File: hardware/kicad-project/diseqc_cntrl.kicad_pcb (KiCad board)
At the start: 4 copper layers, 90 x 100 mm, 124 parts, among them IC1 TPS560200DBVR, IC2 STM32F407VGT6, IC3 USBLC6-2P6, IC4 FM24CL16B-GTR, IC5 LNBH26PQR, IC6 W5500, J1 Barrel Jack, J2 Conn_01x04_Pin, J3 Conn_01x04_Pin, J4 USB4110-GF-A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

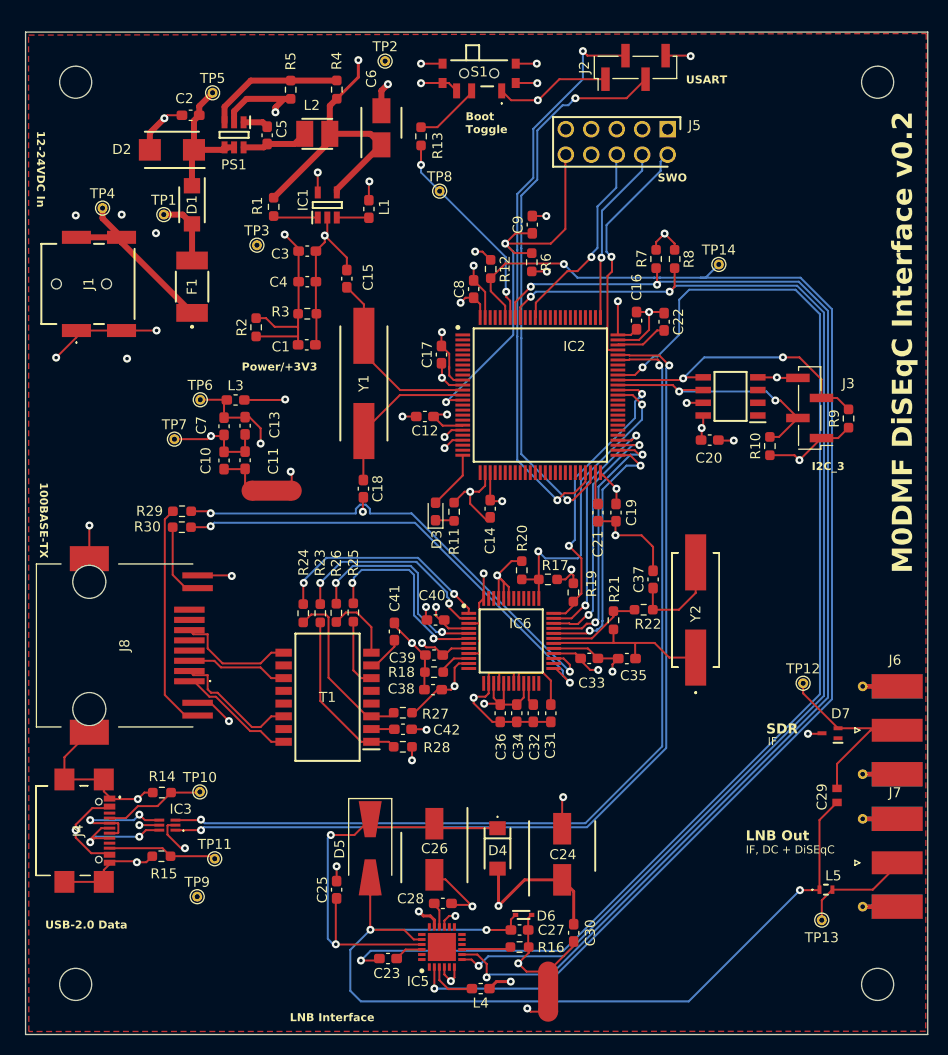
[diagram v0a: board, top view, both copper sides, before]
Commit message: Fixed pin conflict: TIM1_CH1/I2C3_SCL
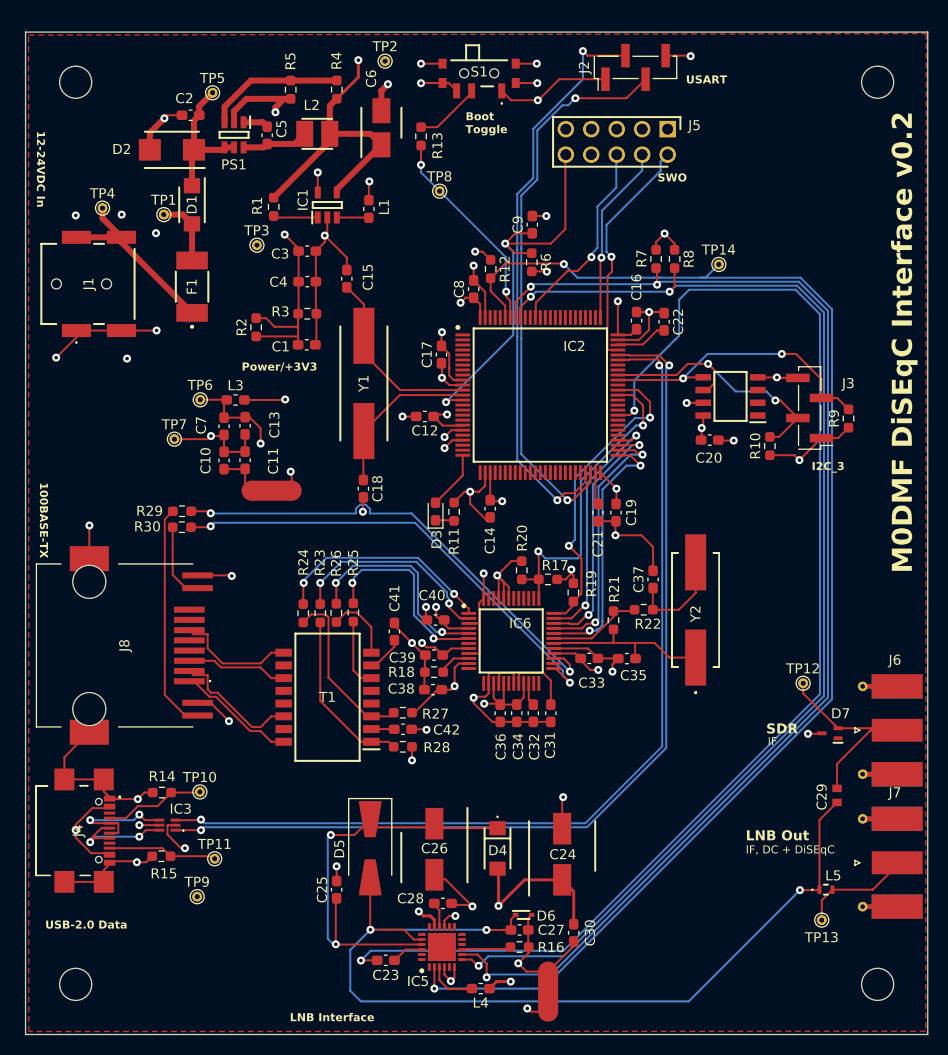
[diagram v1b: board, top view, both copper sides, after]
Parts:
- moved C23 0.28 mm to (85.9, 142.6), turned to 180 degrees
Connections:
- C23 pad 1: Net-(IC2-PA8) -> /MCU/LNBH26PQR/DISEQC
- C23 pad 2: /MCU/TIM1_CH1_DSQ -> /MCU/TIM4_CH1
- IC2 pad 59: unconnected-(IC2-PD12-Pad59) -> /MCU/TIM4_CH1
- IC2 pad 65: /MCU/I2C3_SCL -> unconnected-(IC2-PC8-Pad65)
- IC2 pad 67: Net-(IC2-PA8) -> /MCU/I2C3_SCL
- IC5 pad 22: /MCU/TIM1_CH1_DSQ -> /MCU/LNBH26PQR/DISEQC
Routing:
- net /MCU/TIM4_CH1: track 0.00 -> 127.0 mm, vias 0 -> 2
- net Net-(IC2-PA8): track 123.4 -> 0.00 mm, vias 2 -> 0
- net /MCU/TIM1_CH1_DSQ: track 2.89 -> 0.00 mm
- net /MCU/LNBH26PQR/DISEQC: track 0.00 -> 2.89 mm
- net /MCU/I2C3_SCL: track 25.4 -> 27.8 mm
- net /MCU/W5500 Ethernet/W5500_INT: track 29.6 -> 31.0 mm

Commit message: Grounded additional pins on IC5 & cleaned up track routing
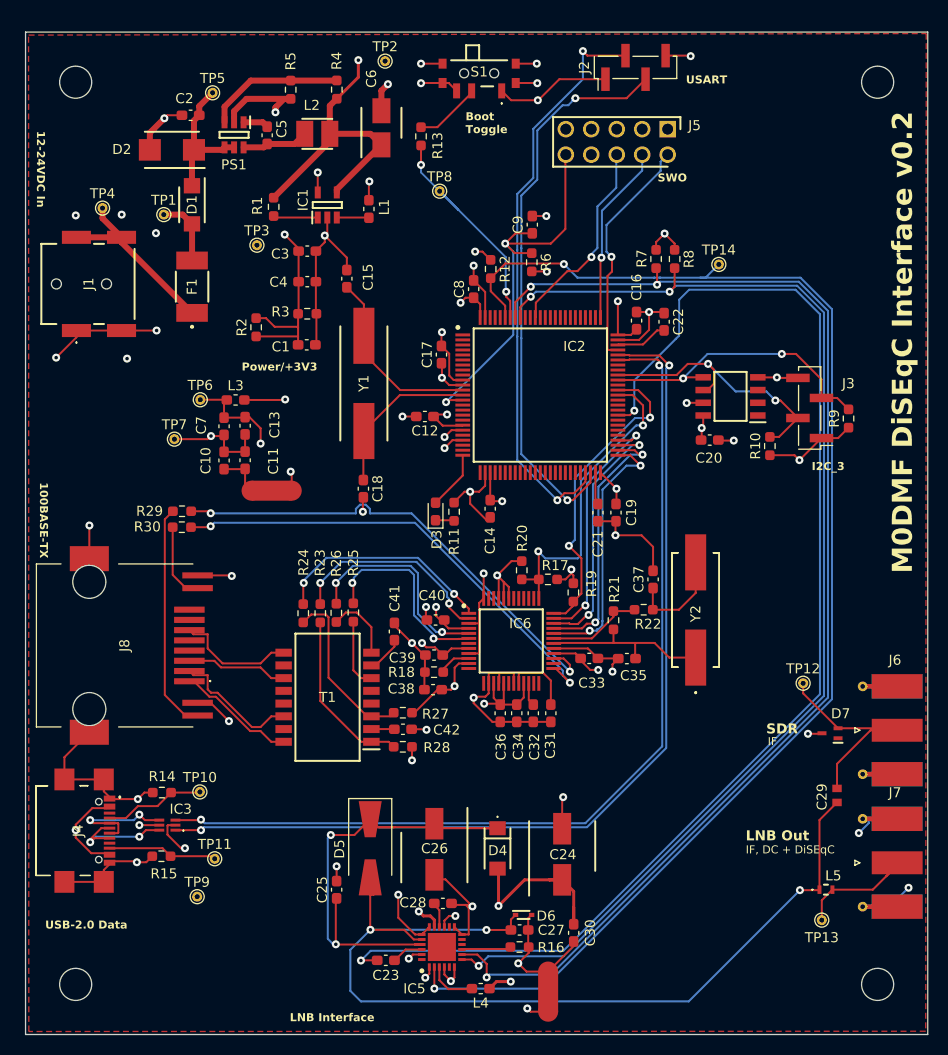
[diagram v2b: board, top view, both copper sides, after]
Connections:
- IC5 pad 1: unconnected-(IC5-DSQOUT_-B-Pad1) -> PGND
- IC5 pad 12: unconnected-(IC5-DETIN-B-Pad12) -> PGND
- IC5 pad 13: unconnected-(IC5-BPSW-B-Pad13) -> PGND
- IC5 pad 18: unconnected-(IC5-BPSW-A-Pad18) -> PGND
- IC5 pad 19: unconnected-(IC5-DETIN-A-Pad19) -> PGND
- IC5 pad 23: unconnected-(IC5-DSQOUT-A-Pad23) -> PGND
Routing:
- net PGND: track 24.7 -> 40.3 mm, vias 4 -> 7
- net GND: track 216.0 -> 230.3 mm, vias 41 -> 43
- net Net-(D4-K): track 42.1 -> 47.1 mm
- net +12V: track 201.2 -> 204.2 mm
- net /MCU/BOOT0: track 20.8 -> 23.4 mm
- net LNB_OUT: track 11.3 -> 13.1 mm
- net IF_OUT: track 23.3 -> 22.2 mm
- net VBUS: track 33.6 -> 34.3 mm
- net TX+: track 12.6 -> 11.9 mm
- net USB_D-: track 95.3 -> 94.7 mm
- net /MCU/W5500 Ethernet/W5500_INT: track 31.0 -> 31.5 mm
- net /MCU/LNBH26PQR/DISEQC: track 2.89 -> 3.41 mm

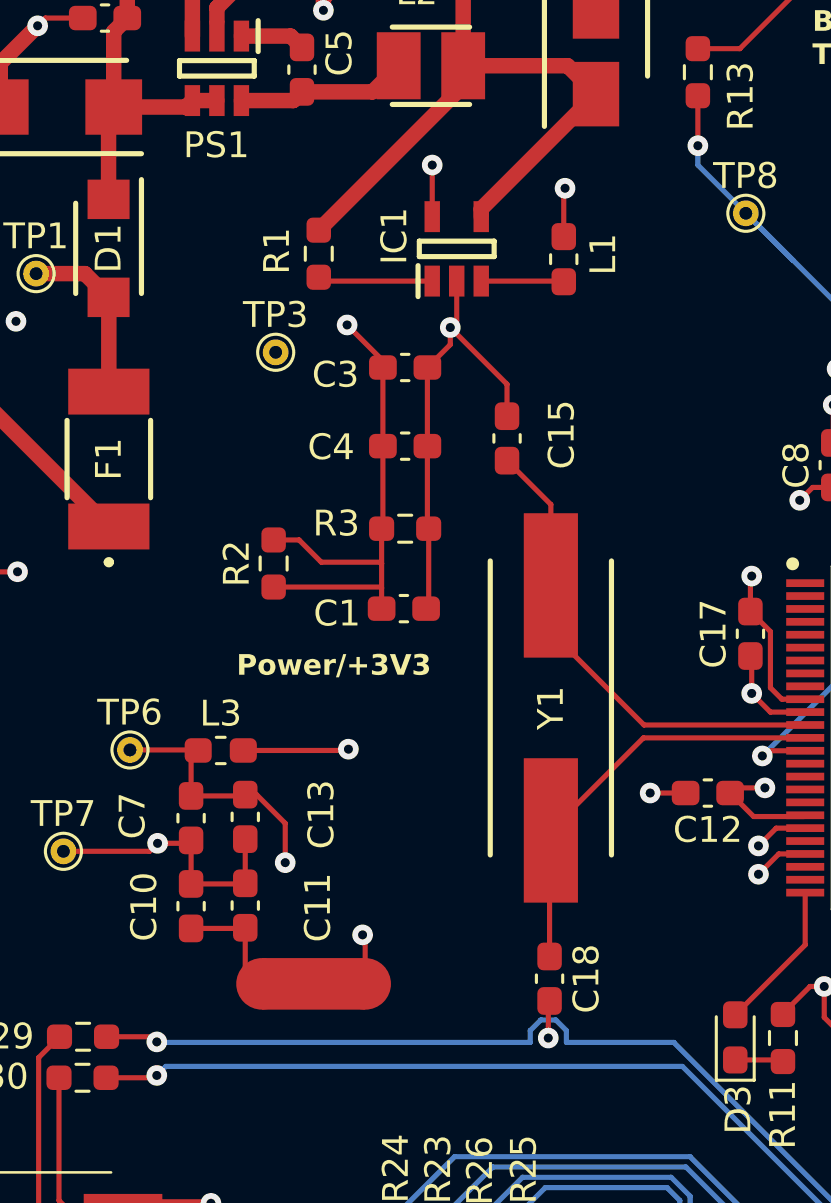
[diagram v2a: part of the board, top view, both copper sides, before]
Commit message: Corrected 3v3 reg component layout
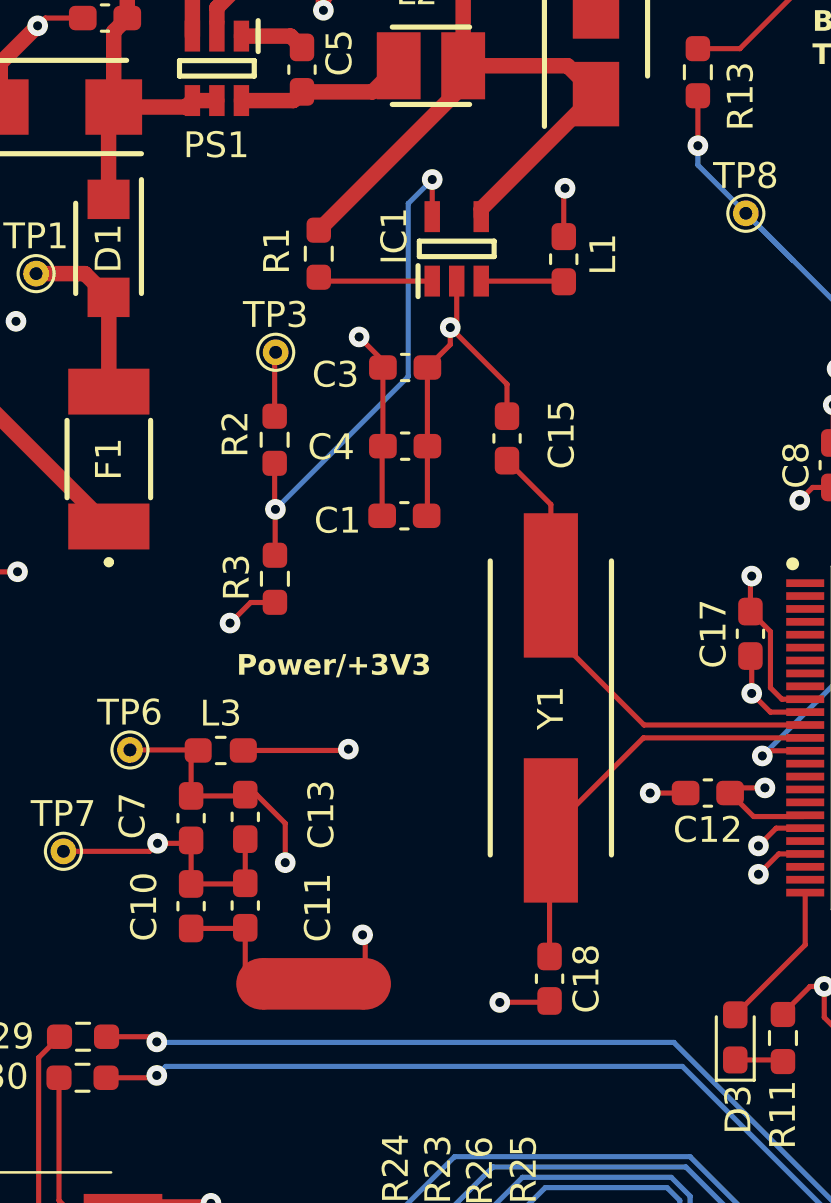
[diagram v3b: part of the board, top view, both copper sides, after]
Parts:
- moved R3 5.41 mm to (73.0, 80.0), turned to -90 degrees
- moved R2 4.80 mm to (73.0, 74.7), turned to -90 degrees
- moved C1 3.60 mm to (78.1, 77.6)
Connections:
- IC1 pad 5: +3V3 -> Net-(IC1-VSENSE)
- R2 pad 2: +3V3 -> Net-(IC1-VSENSE)
- R3 pad 1: +3V3 -> Net-(IC1-VSENSE)
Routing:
- net Net-(IC1-VSENSE): track 0.00 -> 20.4 mm, vias 0 -> 2
- net +3V3: track 145.1 -> 132.8 mm, vias 26 -> 25
- net /MCU/W5500 Ethernet/ACTLED: track 48.3 -> 47.0 mm
- net GND: track 230.3 -> 229.2 mm, vias 43 -> 44

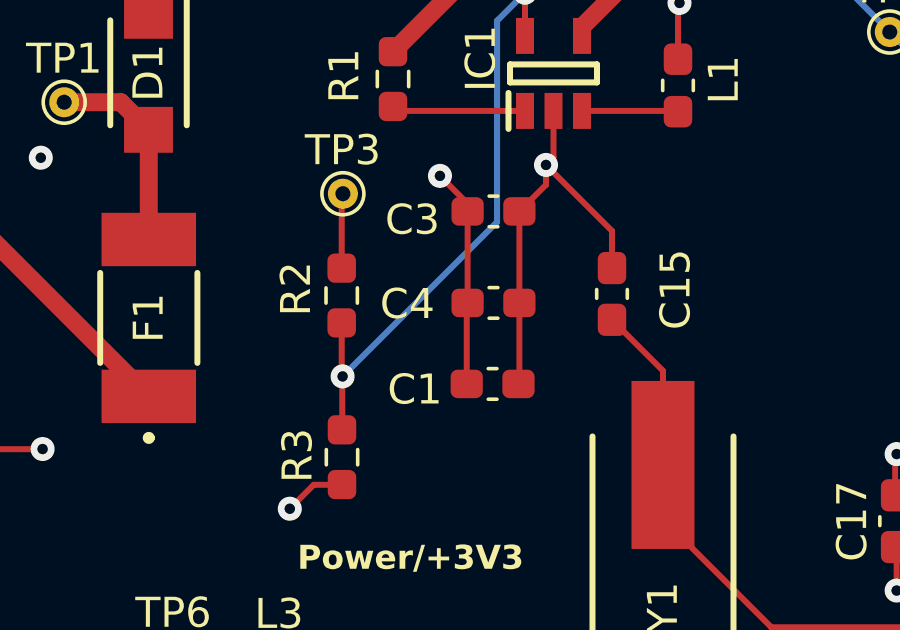
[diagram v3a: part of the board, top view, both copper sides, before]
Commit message: Removed/rerouted optional component C4
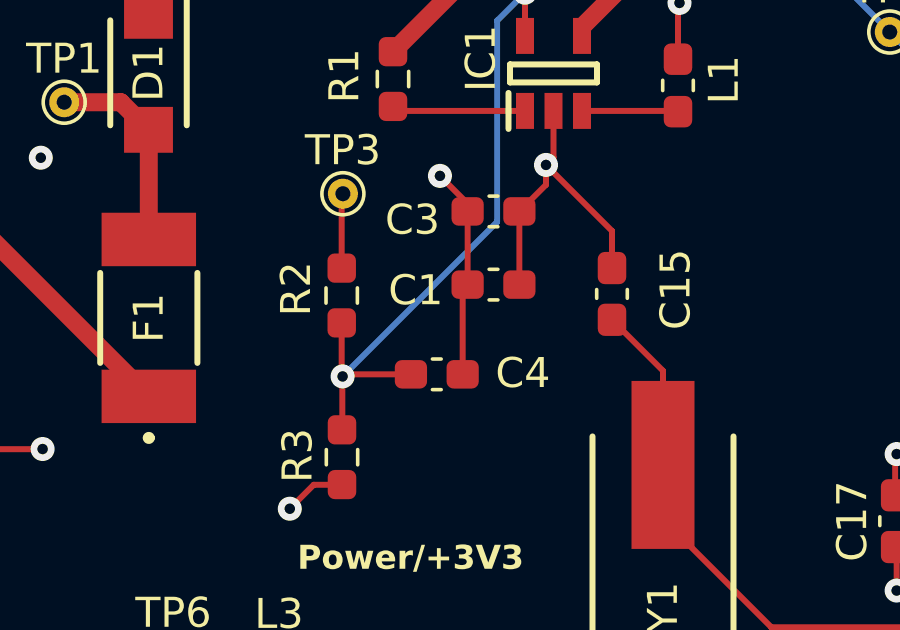
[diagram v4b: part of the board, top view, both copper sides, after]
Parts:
- C4: value 1u -> 22pF DNP
- moved C1 3.31 mm to (78.1, 74.3)
- moved C4 3.04 mm to (76.2, 77.3), turned to 180 degrees
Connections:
- C4 pad 2: GND -> Net-(IC1-VSENSE)
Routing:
- net GND: track 229.2 -> 225.9 mm
- net Net-(IC1-VSENSE): track 20.4 -> 22.7 mm
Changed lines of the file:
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@@
 	(footprint "Capacitor_SMD:C_0603_1608Metric_Pad1.08x0.95mm_HandSolder"
 		(layer "F.Cu")
-		(at 78.07 77.6)
+		(at 78.1 74.29)
 		(descr "Capacitor SMD 0603 (1608 Metric), square (rectangular) end terminal, IPC-7351 nominal with elongated pad for handsoldering. (Body size source: IPC-SM-782 page 76, https://www.pcb-3d.com/wordpress/wp-content/uploads/ipc-sm-782a_amendment_1_and_2.pdf), generated with kicad-footprint-generator")
 		(tags "capacitor handsolder")
@@
 	(footprint "Capacitor_SMD:C_0603_1608Metric_Pad1.08x0.95mm_HandSolder"
 		(layer "F.Cu")
-		(at 78.1 74.9)
+		(at 76.21 77.28 180)
 		(descr "Capacitor SMD 0603 (1608 Metric), square (rectangular) end terminal, IPC-7351 nominal with elongated pad for handsoldering. (Body size source: IPC-SM-782 page 76, https://www.pcb-3d.com/wordpress/wp-content/uploads/ipc-sm-782a_amendment_1_and_2.pdf), generated with kicad-footprint-generator")
 		(tags "capacitor handsolder")
@@
 			)
 		)
-		(property "Value" "1u"
+		(property "Value" "22pF DNP"
 			(at 0 1.43 0)
 			(layer "F.Fab")
@@
 		)
 		(property "Manufacturer_Part_Number" "C2012X7R1E105ZK125AB"
-			(at 0 0 0)
+			(at 0 0 180)
 			(unlocked yes)
 			(layer "F.Fab")
@@
 		)
 		(property "Maufacturer_Part_Number" ""
-			(at 0 0 0)
+			(at 0 0 180)
 			(unlocked yes)
 			(layer "F.Fab")
@@
 		)
 		(property "Manufacturer_Part_Code" ""
-			(at 0 0 0)
+			(at 0 0 180)
 			(unlocked yes)
 			(layer "F.Fab")
@@
 		)
 		(property "Mouser_Part_Number" ""
-			(at 0 0 0)
+			(at 0 0 180)
 			(unlocked yes)
 			(layer "F.Fab")
@@
 		)
 		(property "Mouser Part Number" "81-GRM39R105K10"
-			(at 0 0 0)
+			(at 0 0 180)
 			(unlocked yes)
 			(layer "F.Fab")
@@
 		(sheetname "/")
 		(sheetfile "diseqc_cntrl.kicad_sch")
-		(attr smd)
+		(attr smd exclude_from_bom dnp)
 		(fp_line
-			(start -0.146267 -0.51)
-			(end 0.146267 -0.51)
+			(start -0.146267 0.51)
+			(end 0.146267 0.51)
 			(stroke
 				(width 0.12)
@@
 		)
 		(fp_line
-			(start -0.146267 0.51)
-			(end 0.146267 0.51)
+			(start -0.146267 -0.51)
+			(end 0.146267 -0.51)
 			(stroke
 				(width 0.12)
@@
 		)
 		(pad "1" smd roundrect
-			(at -0.8625 0)
+			(at -0.8625 0 180)
 			(size 1.075 0.95)
 			(layers "F.Cu" "F.Mask" "F.Paste")
@@
 		)
 		(pad "2" smd roundrect
-			(at 0.8625 0)
+			(at 0.8625 0 180)
 			(size 1.075 0.95)
 			(layers "F.Cu" "F.Mask" "F.Paste")
 			(roundrect_rratio 0.25)
-			(net 1 "GND")
+			(net 180 "Net-(IC1-VSENSE)")
 			(pintype "passive")
 		)
@@
 	)
 	(segment
+		(start 78.9625 71.85)
+		(end 78.9625 74.29)
+		(width 0.2)
+		(layer "F.Cu")
+		(net 1)
+	)
+	(segment
 		(start 64.156 130.066)
 		(end 65.505 131.415)
@@
 	)
 	(segment
-		(start 78.9625 74.9)
-		(end 78.9625 77.57)
-		(width 0.2)
-		(layer "F.Cu")
-		(net 1)
-	)
-	(segment
 		(start 65.6 58.3)
 		(end 64.15 58.3)
@@
 	)
 	(segment
-		(start 78.9625 71.85)
-		(end 78.9625 74.9)
-		(width 0.2)
-		(layer "F.Cu")
-		(net 1)
-	)
-	(segment
 		(start 65.6 58.55)
 		(end 65.6 58.3)
@@
 	)
 	(segment
-		(start 78.9625 77.57)
-		(end 78.9325 77.6)
-		(width 0.2)
-		(layer "F.Cu")
-		(net 1)
-	)
-	(segment
 		(start 97.2 114.976)
 		(end 97.249 114.927)
@@
 	)
 	(segment
-		(start 77.2075 77.6)
-		(end 77.2075 74.93)
+		(start 91.5125 115.6)
+		(end 92.45 115.6)
 		(width 0.2)
 		(layer "F.Cu")
@@
 	)
 	(segment
-		(start 91.5125 115.6)
-		(end 92.45 115.6)
+		(start 98.475 102.775)
+		(end 97.05 104.2)
 		(width 0.2)
 		(layer "F.Cu")
@@
 	)
 	(segment
-		(start 98.475 102.775)
-		(end 97.05 104.2)
+		(start 77.0725 74.455)
+		(end 77.2375 74.29)
 		(width 0.2)
 		(layer "F.Cu")
@@
 	)
 	(segment
-		(start 77.2375 71.85)
-		(end 77.2375 74.9)
-		(width 0.2)
-		(layer "F.Cu")
-		(net 2)
-	)
-	(segment
 		(start 67.16 104.2)
 		(end 70.51 104.2)
@@
 	)
 	(segment
-		(start 77.2075 74.93)
-		(end 77.2375 74.9)
-		(width 0.2)
-		(layer "F.Cu")
-		(net 2)
-	)
-	(segment
 		(start 91.538 84.488)
 		(end 92.262 85.212)
@@
 	)
 	(segment
+		(start 77.0725 77.28)
+		(end 77.0725 74.455)
+		(width 0.2)
+		(layer "F.Cu")
+		(net 2)
+	)
+	(segment
 		(start 126.712 92.2125)
 		(end 124.25 92.2125)
@@
 	)
 	(segment
+		(start 77.2375 71.85)
+		(end 77.2375 74.29)
+		(width 0.2)
+		(layer "F.Cu")
+		(net 2)
+	)
+	(segment
 		(start 93.9 76.5)
 		(end 93.4 77)
@@
 	)
 	(segment
+		(start 73.14 77.28)
+		(end 73.07 77.35)
+		(width 0.2)
+		(layer "F.Cu")
+		(net 180)
+	)
+	(segment
 		(start 73.02 79.1375)
 		(end 73.06 79.0975)
@@
 		(width 0.2)
 		(layer "F.Cu")
+		(net 180)
+	)
+	(segment
+		(start 75.3475 77.28)
+		(end 73.14 77.28)
+		(width 0.2)
+		(layer "F.Cu")
